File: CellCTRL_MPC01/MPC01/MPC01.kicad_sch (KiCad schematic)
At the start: 51 parts, among them J1 Power 24V, J10 Microstepping, J11 Microstepping, J12 StepMotor 1, J13 StepMotor 2, J14 StepMotor 3, J15 StepMotor 4, J16 Conn_01x05_Pin, J2 Conn_01x03_Pin, J3 Servo Motor 1u2, J4 Endstop X, J5 Endstop Y, J6 Endstop Z, J7 0Ohm Jumper, J8 Microstepping, J9 Microstepping, U1 TP8485E-SR

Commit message: Update der PCBs
MPC01: Update der Schematics (Lötbrücken anstatt von Steckbrücken bei MSN und generell Brücken bei PDNUart)
MPC-Status: Fertigstellen des PCBs
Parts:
- removed J10, J11, J8, J9: Microstepping, MPC01_lib:PinHeader_2x03_P2.54mm_Vertical_ Pinorder, symbol Connector_Generic:Conn_02x03_Counter_Clockwise
- removed R10, R8: 1K, Resistor_SMD:R_0805_2012Metric_Pad1.20x1.40mm_HandSolder, symbol Device:R
- added 10K1, 10K2, 10K3, 10K4, 10K5, 10K6, 10K7, 10K8, R4, R5: 1K, Resistor_SMD:R_0805_2012Metric_Pad1.20x1.40mm_HandSolder, symbol Device:R
- added JP1, JP10, JP4, JP7: MS1, Connector_PinSocket_2.54mm:PinSocket_1x02_P2.54mm_Vertical, symbol Jumper:Jumper_2_Open
- added JP11, JP2, JP5, JP8: MS2, Connector_PinSocket_2.54mm:PinSocket_1x02_P2.54mm_Vertical, symbol Jumper:Jumper_2_Open
- added JP13, JP3, JP6, JP9: Jumper_3_Open, symbol Jumper:Jumper_3_Open
- J6: renamed from J16; value Conn_01x05_Pin -> I2C
- renumbered A2 to A1, A3 to A2, A1 to A3, C2 to C1, C5 to C10, C9 to C11, C13 to C12, C1 to C13, C6 to C2, C10 to C3, C3 to C4, C7 to C5, C11 to C6, C4 to C7, C12 to C9, D3 to D2, D2 to D3, J15 to J10, J5 to J11, J6 to J12, J3 to J2, J12 to J3, J7 to J4, J13 to J5, J14 to J7, J4 to J8, J2 to J9, JP1 to JP12, R7 to R1, R3 to R10, R5 to R2, R6 to R3, R1 to R6, R4 to R7, R2 to R8
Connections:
- net 5V: now also JP1.2 (B), JP10.2 (B), JP11.2 (B), JP2.2 (B), JP4.2 (B), JP5.2 (B), JP7.2 (B), JP8.2 (B)
- net GND: now also 10K1.1, 10K2.1, 10K3.1, 10K4.1, 10K5.1, 10K6.1, 10K7.1, 10K8.1
- net PDNUart: now also R1.2, R9.2, R4.2, R5.2; no longer R1.1, R9.1
- net at A2.4 (RX): now also JP6.1 (A)
- net at A2.2 (MS1): now also 10K4.2, JP5.1 (A)
- net at A2.3 (MS2): now also 10K3.2, JP4.1 (A)
- net at A2.5 (TX): now also JP6.3 (B)
- net at A1.4 (RX): now also JP3.1 (A); no longer R1.2
- net at A4.4 (RX): now also JP9.1 (A); no longer R9.2
- net at A5.4 (RX): now also JP13.1 (A)
- net at A5.2 (MS1): now also 10K8.2, JP11.1 (A)
- net at A5.3 (MS2): now also 10K7.2, JP10.1 (A)
- net at A5.5 (TX): now also JP13.3 (B)
- net at A1.2 (MS1): now also 10K2.2, JP2.1 (A)
- net at A1.3 (MS2): now also 10K1.2, JP1.1 (A)
- net at A1.5 (TX): now also JP3.3 (B)
- net at A4.2 (MS1): now also 10K6.2, JP8.1 (A)
- net at A4.3 (MS2): now also 10K5.2, JP7.1 (A)
- net at A4.5 (TX): now also JP9.3 (B)
- new net: JP9.2 (C), R5.1
- new net: JP3.2 (C), R1.1
- new net: JP6.2 (C), R4.1
- new net: JP13.2 (C), R9.1
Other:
- moved on the sheet: A3, J6, R1

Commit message: New schematics
Many Changes:)
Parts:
- removed 10K7, 10K8, R9: 1K, Resistor_SMD:R_0805_2012Metric_Pad1.20x1.40mm_HandSolder, symbol Device:R
- removed A5: TMC2209, MPC01_lib:TMC2209, symbol MPC01_Lib:BIGTREETECH_TMC2209_V1.3_Stepper_Motor_Driver
- removed C10: 100uf, Capacitor_SMD:CP_Elec_6.3x7.7, symbol Device:C_Polarized_US
- removed C11: 1uF, Capacitor_SMD:C_0805_2012Metric_Pad1.18x1.45mm_HandSolder, symbol PCM_SparkFun-Capacitor:C
- removed C12: 4,7uF, Capacitor_SMD:C_0805_2012Metric_Pad1.18x1.45mm_HandSolder, symbol PCM_SparkFun-Capacitor:C
- removed J10: StepMotor 4, Connector_JST:JST_XH_B4B-XH-A_1x04_P2.50mm_Vertical, symbol Connector:Conn_01x04_Pin
- removed J6: I2C, Connector_PinHeader_2.54mm:PinHeader_1x05_P2.54mm_Vertical, symbol Connector:Conn_01x05_Pin
- removed JP10: MS1, Connector_PinSocket_2.54mm:PinSocket_1x02_P2.54mm_Vertical, symbol Jumper:Jumper_2_Open
- removed JP11: MS2, Connector_PinSocket_2.54mm:PinSocket_1x02_P2.54mm_Vertical, symbol Jumper:Jumper_2_Open
- removed JP13: Jumper_3_Open, symbol Jumper:Jumper_3_Open
- added J13: I2C, symbol Connector:Conn_01x05_Pin
- added J14: Enable/Disable, symbol Connector:Conn_01x02_Pin
- added R11: 1K, Resistor_SMD:R_0805_2012Metric_Pad1.20x1.40mm_HandSolder, symbol Device:R
- added R12: 10K, Resistor_SMD:R_0805_2012Metric_Pad1.20x1.40mm_HandSolder, symbol Device:R
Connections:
- net DIR4 is gone; now on net DIR3: A3.D6
- net STEP4 is gone; now on net STEP3: A3.D7
- net +24V: now also J13.3 (Pin_3)
- net 5V: now also J13.5 (Pin_5), R12.2
- net DIR3: no longer A3.D4
- net ENABLE: now also J14.1 (Pin_1), R11.1, R12.1; no longer A3.D1 (D1/TX)
- net GND: now also J13.4 (Pin_4), J14.2 (Pin_2)
- net RS485_RX: now also A3.A4; no longer A3.D8
- net RS485_TX: now also A3.A5; no longer A3.D9
- net RX: now also A3.D9; no longer A3.A5
- net STEP3: no longer A3.D5
- net TX: now also A3.D8; no longer A3.A4
- new net: A3.D4, J13.2 (Pin_2)
- new net: A3.D5, J13.1 (Pin_1)
- new net ENABLEOut: A3.D1 (D1/TX)
- new net ENABLE_Out: R11.2
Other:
- note added: "DC-Buck Converter"
- note added: "Enable (NotAus)"
- moved on the sheet: A3, BC1, C13, D1, D2, D3, F1, J1, J11, J12, J2, J4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

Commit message: Update MPC01
MPC01 update
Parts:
- removed 10K1, 10K2, 10K3, 10K4, 10K5, 10K6: 1K, Resistor_SMD:R_0805_2012Metric_Pad1.20x1.40mm_HandSolder, symbol Device:R
- removed J2: Servo Motor 1u2, Connector_JST:JST_XH_B5B-XH-A_1x05_P2.50mm_Vertical, symbol Connector:Conn_01x05_Pin
- added R1, R2, R3, R4, R5, R6: 10K, Resistor_SMD:R_0805_2012Metric_Pad1.20x1.40mm_HandSolder, symbol Device:R
- J10: renamed from J14; footprint (none) -> Connector_JST:JST_XH_B2B-XH-A_1x02_P2.50mm_Vertical
- J5: renamed from J13; footprint (none) -> Connector_JST:JST_XH_B5B-XH-A_1x05_P2.50mm_Vertical
- JP1, JP5: footprint Connector_PinSocket_2.54mm:PinSocket_1x02_P2.54mm_Vertical -> Connector_PinHeader_2.54mm:PinHeader_1x02_P2.54mm_Vertical
- JP2: renamed from JP4; footprint Connector_PinSocket_2.54mm:PinSocket_1x02_P2.54mm_Vertical -> Connector_PinHeader_2.54mm:PinHeader_1x02_P2.54mm_Vertical
- JP3: renamed from JP7; footprint Connector_PinSocket_2.54mm:PinSocket_1x02_P2.54mm_Vertical -> Connector_PinHeader_2.54mm:PinHeader_1x02_P2.54mm_Vertical
- JP4: renamed from JP2; footprint Connector_PinSocket_2.54mm:PinSocket_1x02_P2.54mm_Vertical -> Connector_PinHeader_2.54mm:PinHeader_1x02_P2.54mm_Vertical
- JP6: renamed from JP8; footprint Connector_PinSocket_2.54mm:PinSocket_1x02_P2.54mm_Vertical -> Connector_PinHeader_2.54mm:PinHeader_1x02_P2.54mm_Vertical
- JP7: renamed from JP3; footprint (none) -> PCM_SparkFun-Jumper:Jumper_3_NO
- JP8: renamed from JP6; footprint (none) -> PCM_SparkFun-Jumper:Jumper_3_NO
- JP9: footprint (none) -> PCM_SparkFun-Jumper:Jumper_3_NO
- renumbered A4 to A3, A3 to A4, C13 to C10, D3 to D1, D1 to D2, D2 to D3, J3 to J1, J12 to J11, J5 to J2, J7 to J3, J9 to J4, J8 to J6, J1 to J7, J4 to J8, J11 to J9, JP12 to JP10, R6 to R10, R7 to R11, R8 to R12, R10 to R13, R12 to R14, R11 to R15, R2 to R16, R3 to R17, R1 to R7, R4 to R8, R5 to R9
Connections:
- net ENABLE_Out is gone; now on net ENABLEOut: R15.2
- net Motor1 is gone; now on net DIR3: A4.D2 (D2_INT0)
- net Motor2 is gone; now on net STEP3: A4.D3 (D3_INT1)
- net DIR1: now also A4.D6; no longer A4.D12
- net DIR2: now also A4.D4; no longer A4.D10 (D10_CS)
- net DIR3: no longer A4.D6
- net ENABLEOut: now also A4.D13; no longer A4.D1 (D1/TX)
- net GND: now also R1.1, R2.1, R3.1, R4.1, R5.1, R6.1
- net PGOOD: now also A4.D12; no longer A4.D0 (D0/RX)
- net RS485_RX: now also A4.D11; no longer A4.A4
- net RS485_TX: now also A4.D10 (D10_CS); no longer A4.A5
- net STEP1: now also A4.D7; no longer A4.D13
- net STEP2: now also A4.D5; no longer A4.D11
- net STEP3: no longer A4.D7
- net at A3.3 (MS2), JP3.1 (A): now also R5.2
- net at A2.2 (MS1), JP5.1 (A): now also R1.2
- net at A2.3 (MS2), JP2.1 (A): now also R4.2
- net at A1.3 (MS2), JP1.1 (A): now also R2.2
- net at J5.2 (Pin_2): now also A4.A4; no longer A4.D4
- net at J5.1 (Pin_1): now also A4.A5; no longer A4.D5
- net at A3.2 (MS1), JP6.1 (A): now also R6.2
- net at A1.2 (MS1), JP4.1 (A): now also R3.2
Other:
- note removed: "Servo Motor TurningUnit + Gripper"
- moved on the sheet: A1, A2, A3, A4, BC1, C1, C10, C2, C3, C4, C5, C6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

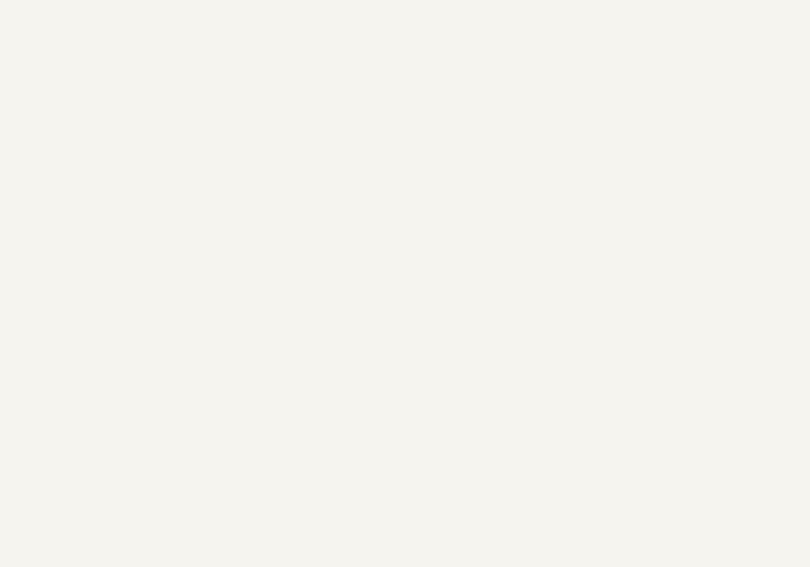
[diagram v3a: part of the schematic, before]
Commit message: Mounting Hole adds
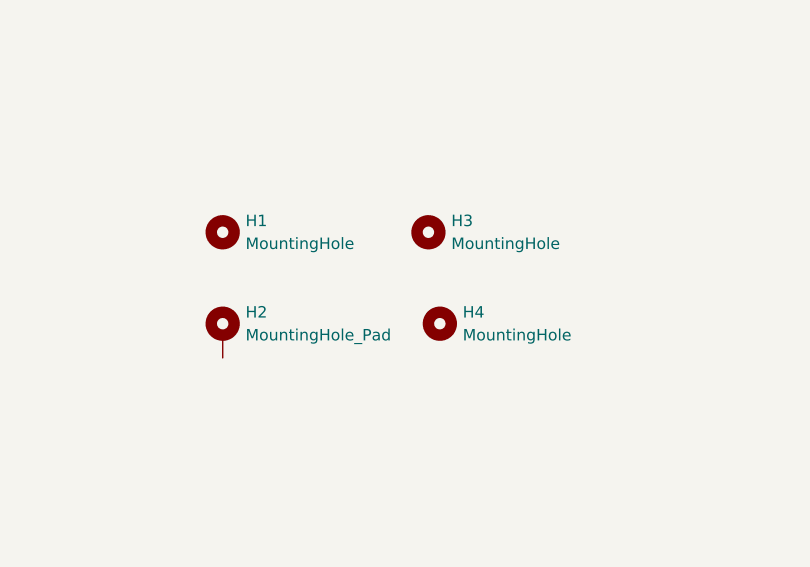
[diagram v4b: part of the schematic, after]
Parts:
- added H1, H3, H4: MountingHole, MountingHole:MountingHole_2.2mm_M2_DIN965, symbol Mechanical:MountingHole
- added H2: MountingHole_Pad, MountingHole:MountingHole_2.2mm_M2_DIN965_Pad, symbol Mechanical:MountingHole_Pad

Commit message: Maße
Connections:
- net at A4.A4: now also J5.1 (Pin_1); no longer J5.2 (Pin_2)
- net at A4.A5: now also J5.2 (Pin_2); no longer J5.1 (Pin_1)
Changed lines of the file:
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@@
+	(wire
+		(pts
+			(xy 171.45 113.03) (xy 171.45 115.57)
+		)
+		(stroke
+			(width 0)
+			(type default)
+		)
+	)
 	(wire
 		(pts
@@
 	(wire
 		(pts
+			(xy 168.91 115.57) (xy 168.91 114.3)
+		)
+		(stroke
+			(width 0)
+			(type default)
+		)
+	)
+	(wire
+		(pts
 			(xy 179.07 189.23) (xy 175.26 189.23)
 		)
@@
 	(wire
 		(pts
+			(xy 168.91 114.3) (xy 173.99 114.3)
+		)
+		(stroke
+			(width 0)
+			(type default)
+		)
+	)
+	(wire
+		(pts
 			(xy 95.25 29.21) (xy 95.25 26.67)
 		)
@@
 	(wire
 		(pts
-			(xy 154.94 113.03) (xy 191.77 113.03)
-		)
-		(stroke
-			(width 0)
-			(type default)
-		)
-	)
-	(wire
-		(pts
 			(xy 242.57 105.41) (xy 246.38 105.41)
 		)
@@
 	(wire
 		(pts
+			(xy 171.45 115.57) (xy 191.77 115.57)
+		)
+		(stroke
+			(width 0)
+			(type default)
+		)
+	)
+	(wire
+		(pts
 			(xy 72.39 111.76) (xy 72.39 109.22)
 		)
@@
 	(wire
 		(pts
+			(xy 154.94 113.03) (xy 171.45 113.03)
+		)
+		(stroke
+			(width 0)
+			(type default)
+		)
+	)
+	(wire
+		(pts
 			(xy 204.47 49.53) (xy 193.04 49.53)
 		)
@@
 	(wire
 		(pts
-			(xy 154.94 115.57) (xy 191.77 115.57)
+			(xy 154.94 115.57) (xy 168.91 115.57)
 		)
 		(stroke
@@
 	(wire
 		(pts
+			(xy 173.99 113.03) (xy 191.77 113.03)
+		)
+		(stroke
+			(width 0)
+			(type default)
+		)
+	)
+	(wire
+		(pts
 			(xy 242.57 97.79) (xy 246.38 97.79)
 		)
@@
 		)
 		(stroke
+			(width 0)
+			(type default)
+		)
+	)
+	(wire
+		(pts
+			(xy 173.99 114.3) (xy 173.99 113.03)
+		)
+		(stroke

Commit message: Fertig V0.1_MPC01
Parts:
- removed H1, H3, H4: MountingHole, MountingHole:MountingHole_2.2mm_M2_DIN965, symbol Mechanical:MountingHole
- added H1, H3, H4: MountingHole_Pad, MountingHole:MountingHole_2.2mm_M2_DIN965_Pad, symbol Mechanical:MountingHole_Pad
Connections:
- net GND: now also H2.1, H1.1, H3.1, H4.1
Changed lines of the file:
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@@
 	)
 	(junction
+		(at 295.91 116.84)
+		(diameter 0)
+		(color 0 0 0 0)
+	)
+	(junction
+		(at 318.77 116.84)
+		(diameter 0)
+		(color 0 0 0 0)
+	)
+	(junction
 		(at 284.48 199.39)
 		(diameter 0)
@@
 	(wire
 		(pts
+			(xy 295.91 114.3) (xy 295.91 116.84)
+		)
+		(stroke
+			(width 0)
+			(type default)
+		)
+	)
+	(wire
+		(pts
 			(xy 142.24 25.4) (xy 146.05 25.4)
 		)
@@
 	(wire
 		(pts
+			(xy 295.91 116.84) (xy 295.91 119.38)
+		)
+		(stroke
+			(width 0)
+			(type default)
+		)
+	)
+	(wire
+		(pts
 			(xy 271.78 41.91) (xy 287.02 41.91)
 		)
@@
 	(wire
 		(pts
+			(xy 318.77 114.3) (xy 318.77 116.84)
+		)
+		(stroke
+			(width 0)
+			(type default)
+		)
+	)
+	(wire
+		(pts
 			(xy 326.39 36.83) (xy 326.39 35.56)
 		)
@@
 	(wire
 		(pts
+			(xy 271.78 116.84) (xy 295.91 116.84)
+		)
+		(stroke
+			(width 0)
+			(type default)
+		)
+	)
+	(wire
+		(pts
 			(xy 20.32 46.99) (xy 22.86 46.99)
 		)
@@
 	(wire
 		(pts
+			(xy 318.77 116.84) (xy 342.9 116.84)
+		)
+		(stroke
+			(width 0)
+			(type default)
+		)
+	)
+	(wire
+		(pts
 			(xy 179.07 210.82) (xy 175.26 210.82)
 		)
@@
 	(wire
 		(pts
+			(xy 271.78 114.3) (xy 271.78 116.84)
+		)
+		(stroke
+			(width 0)
+			(type default)
+		)
+	)
+	(wire
+		(pts
 			(xy 187.96 125.73) (xy 191.77 125.73)
 		)
@@
 	(wire
 		(pts
+			(xy 295.91 116.84) (xy 318.77 116.84)
+		)
+		(stroke
+			(width 0)
+			(type default)
+		)
+	)
+	(wire
+		(pts
 			(xy 49.53 100.33) (xy 49.53 102.87)
 		)
@@
 	(wire
 		(pts
+			(xy 342.9 114.3) (xy 342.9 116.84)
+		)
+		(stroke
+			(width 0)
+			(type default)
+		)
+	)
+	(wire
+		(pts
 			(xy 204.47 46.99) (xy 193.04 46.99)
 		)
@@
 	)
 	(symbol
-		(lib_id "Mechanical:MountingHole")
-		(at 295.91 100.33 0)
-		(unit 1)
-		(exclude_from_sim no)
-		(in_bom no)
-		(on_board yes)
-		(dnp no)
-		(fields_autoplaced yes)
-		(property "Reference" "H1"
-			(at 298.45 99.0599 0)
-			(effects
-				(font
-					(size 1.27 1.27)
-				)
-				(justify left)
-			)
-		)
-		(property "Value" "MountingHole"
-			(at 298.45 101.5999 0)
-			(effects
-				(font
-					(size 1.27 1.27)
-				)
-				(justify left)
-			)
-		)
-		(property "Footprint" "MountingHole:MountingHole_2.2mm_M2_DIN965"
-			(at 295.91 100.33 0)
-			(effects
-				(font
-					(size 1.27 1.27)
-				)
-				(hide yes)
-			)
-		)
-		(property "Datasheet" "~"
-			(at 295.91 100.33 0)
-			(effects
-				(font
-					(size 1.27 1.27)
-				)
-				(hide yes)
-			)
-		)
-		(property "Description" "Mounting Hole without connection"
-			(at 295.91 100.33 0)
-			(effects
-				(font
-					(size 1.27 1.27)
-				)
-				(hide yes)
-			)
-		)
-		(instances
-			(project ""
-				(path "/1dd7e3fd-ee95-4ca4-af41-f6860023c9ff"
-					(reference "H1")
-					(unit 1)
-				)
-			)
-		)
-	)
-	(symbol
 		(lib_id "PCM_SparkFun-Capacitor:C")
 		(at 214.63 31.75 0)
@@
 	)
 	(symbol
+		(lib_id "Mechanical:MountingHole_Pad")
+		(at 342.9 111.76 0)
+		(unit 1)
+		(exclude_from_sim no)
+		(in_bom no)
+		(on_board yes)
+		(dnp no)
+		(fields_autoplaced yes)
+		(property "Reference" "H4"
+			(at 345.44 109.2199 0)
+			(effects
+				(font
+					(size 1.27 1.27)
+				)
+				(justify left)
+			)
+		)
+		(property "Value" "MountingHole_Pad"
+			(at 345.44 111.7599 0)
+			(effects
+				(font
+					(size 1.27 1.27)
+				)
+				(justify left)
+			)
+		)
+		(property "Footprint" "MountingHole:MountingHole_2.2mm_M2_DIN965_Pad"
+			(at 342.9 111.76 0)
+			(effects
+				(font
+					(size 1.27 1.27)
+				)
+				(hide yes)
+			)
+		)
+		(property "Datasheet" "~"
+			(at 342.9 111.76 0)
+			(effects
+				(font
+					(size 1.27 1.27)
+				)
+				(hide yes)
+			)
+		)
+		(property "Description" "Mounting Hole with connection"
+			(at 342.9 111.76 0)
+			(effects
+				(font
+					(size 1.27 1.27)
+				)
+				(hide yes)
+			)
+		)
+		(pin "1"
+		)
+		(instances
+			(project "MPC01"
+				(path "/1dd7e3fd-ee95-4ca4-af41-f6860023c9ff"
+					(reference "H4")
+					(unit 1)
+				)
+			)
+		)
+	)
+	(symbol
 		(lib_id "Connector:Conn_01x04_Pin")
 		(at 328.93 46.99 180)
@@
 	)
 	(symbol
-		(lib_id "Mechanical:MountingHole")
-		(at 318.77 100.33 0)
+		(lib_id "Mechanical:MountingHole_Pad")
+		(at 271.78 111.76 0)
 		(unit 1)
 		(exclude_from_sim no)
@@
 		(dnp no)
 		(fields_autoplaced yes)
-		(property "Reference" "H3"
-			(at 321.31 99.0599 0)
+		(property "Reference" "H1"
+			(at 274.32 109.2199 0)
 			(effects
 				(font
@@
 			)
 		)
-		(property "Value" "MountingHole"
-			(at 321.31 101.5999 0)
+		(property "Value" "MountingHole_Pad"
+			(at 274.32 111.7599 0)
 			(effects
 				(font
@@
 			)
 		)
-		(property "Footprint" "MountingHole:MountingHole_2.2mm_M2_DIN965"
-			(at 318.77 100.33 0)
+		(property "Footprint" "MountingHole:MountingHole_2.2mm_M2_DIN965_Pad"
+			(at 271.78 111.76 0)
 			(effects
 				(font
@@
 		)
 		(property "Datasheet" "~"
-			(at 318.77 100.33 0)
+			(at 271.78 111.76 0)
 			(effects
 				(font
@@
 			)
 		)
-		(property "Description" "Mounting Hole without connection"
-			(at 318.77 100.33 0)
+		(property "Description" "Mounting Hole with connection"
+			(at 271.78 111.76 0)
 			(effects
 				(font
@@
 			)
 		)
+		(pin "1"
+		)
 		(instances
 			(project "MPC01"
 				(path "/1dd7e3fd-ee95-4ca4-af41-f6860023c9ff"
-					(reference "H3")
+					(reference "H1")
 					(unit 1)
 				)
@@
 	)
 	(symbol
-		(lib_id "Mechanical:MountingHole")
-		(at 320.04 110.49 0)
+		(lib_id "power:GND")
+		(at 295.91 119.38 0)
 		(unit 1)
 		(exclude_from_sim no)
-		(in_bom no)
+		(in_bom yes)
 		(on_board yes)
 		(dnp no)
 		(fields_autoplaced yes)
-		(property "Reference" "H4"
-			(at 322.58 109.2199 0)
+		(property "Reference" "#PWR037"
+			(at 295.91 125.73 0)
 			(effects
 				(font
 					(size 1.27 1.27)
 				)
-				(justify left)
+				(hide yes)
 			)
 		)
-		(property "Value" "MountingHole"
-			(at 322.58 111.7599 0)
+		(property "Value" "GND"
+			(at 295.91 124.46 0)
 			(effects
 				(font
 					(size 1.27 1.27)
 				)
-				(justify left)
 			)
 		)
-		(property "Footprint" "MountingHole:MountingHole_2.2mm_M2_DIN965"
-			(at 320.04 110.49 0)
+		(property "Footprint" ""
+			(at 295.91 119.38 0)
 			(effects
 				(font
@@
 			)
 		)
-		(property "Datasheet" "~"
-			(at 320.04 110.49 0)
+		(property "Datasheet" ""
+			(at 295.91 119.38 0)
 			(effects
 				(font
@@
 			)
 		)
-		(property "Description" "Mounting Hole without connection"
-			(at 320.04 110.49 0)
+		(property "Description" "Power symbol creates a global label with name \"GND\" , ground"
+			(at 295.91 119.38 0)
 			(effects
 				(font
@@
 			)
 		)
+		(pin "1"
+		)
 		(instances
 			(project "MPC01"
 				(path "/1dd7e3fd-ee95-4ca4-af41-f6860023c9ff"
-					(reference "H4")
+					(reference "#PWR037")
 					(unit 1)
 				)
@@
 					(unit 1)
 				)
+			)
+		)
+	)
+	(symbol
+		(lib_id "Mechanical:MountingHole_Pad")
+		(at 318.77 111.76 0)
+		(unit 1)
+		(exclude_from_sim no)
+		(in_bom no)
+		(on_board yes)
+		(dnp no)
+		(fields_autoplaced yes)
+		(property "Reference" "H3"
+			(at 321.31 109.2199 0)
+			(effects
+				(font
+					(size 1.27 1.27)
+				)
+				(justify left)
+			)
+		)
+		(property "Value" "MountingHole_Pad"
+			(at 321.31 111.7599 0)
+			(effects
+				(font
+					(size 1.27 1.27)
+				)
+				(justify left)
+			)
+		)
+		(property "Footprint" "MountingHole:MountingHole_2.2mm_M2_DIN965_Pad"
+			(at 318.77 111.76 0)
+			(effects
+				(font
+					(size 1.27 1.27)
+				)
+				(hide yes)
+			)
+		)
+		(property "Datasheet" "~"
+			(at 318.77 111.76 0)
+			(effects
+				(font
+					(size 1.27 1.27)
+				)
+				(hide yes)
+			)
+		)
+		(property "Description" "Mounting Hole with connection"
+			(at 318.77 111.76 0)
+			(effects
+				(font
+					(size 1.27 1.27)
+				)
+				(hide yes)
+			)
+		)
+		(pin "1"
+		)
+		(instances
+			(project "MPC01"
+				(path "/1dd7e3fd-ee95-4ca4-af41-f6860023c9ff"
+					(reference "H3")
+					(unit 1)
+				)
